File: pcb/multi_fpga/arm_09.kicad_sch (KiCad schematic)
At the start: 16 parts, among them U73 IM72D128V01XTMA1, U74 IM72D128V01XTMA1, U75 IM72D128V01XTMA1, U76 IM72D128V01XTMA1, U77 IM72D128V01XTMA1, U78 IM72D128V01XTMA1, U79 IM72D128V01XTMA1, U80 IM72D128V01XTMA1

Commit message: Fixed library and power issues.
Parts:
- C73, C74, C75, C76, C77, C78, C79, C80: symbol C -> multi_fpga:C
- U73, U74, U75, U76, U77, U78, U79, U80: symbol IM72D128 -> multi_fpga:IM72D128

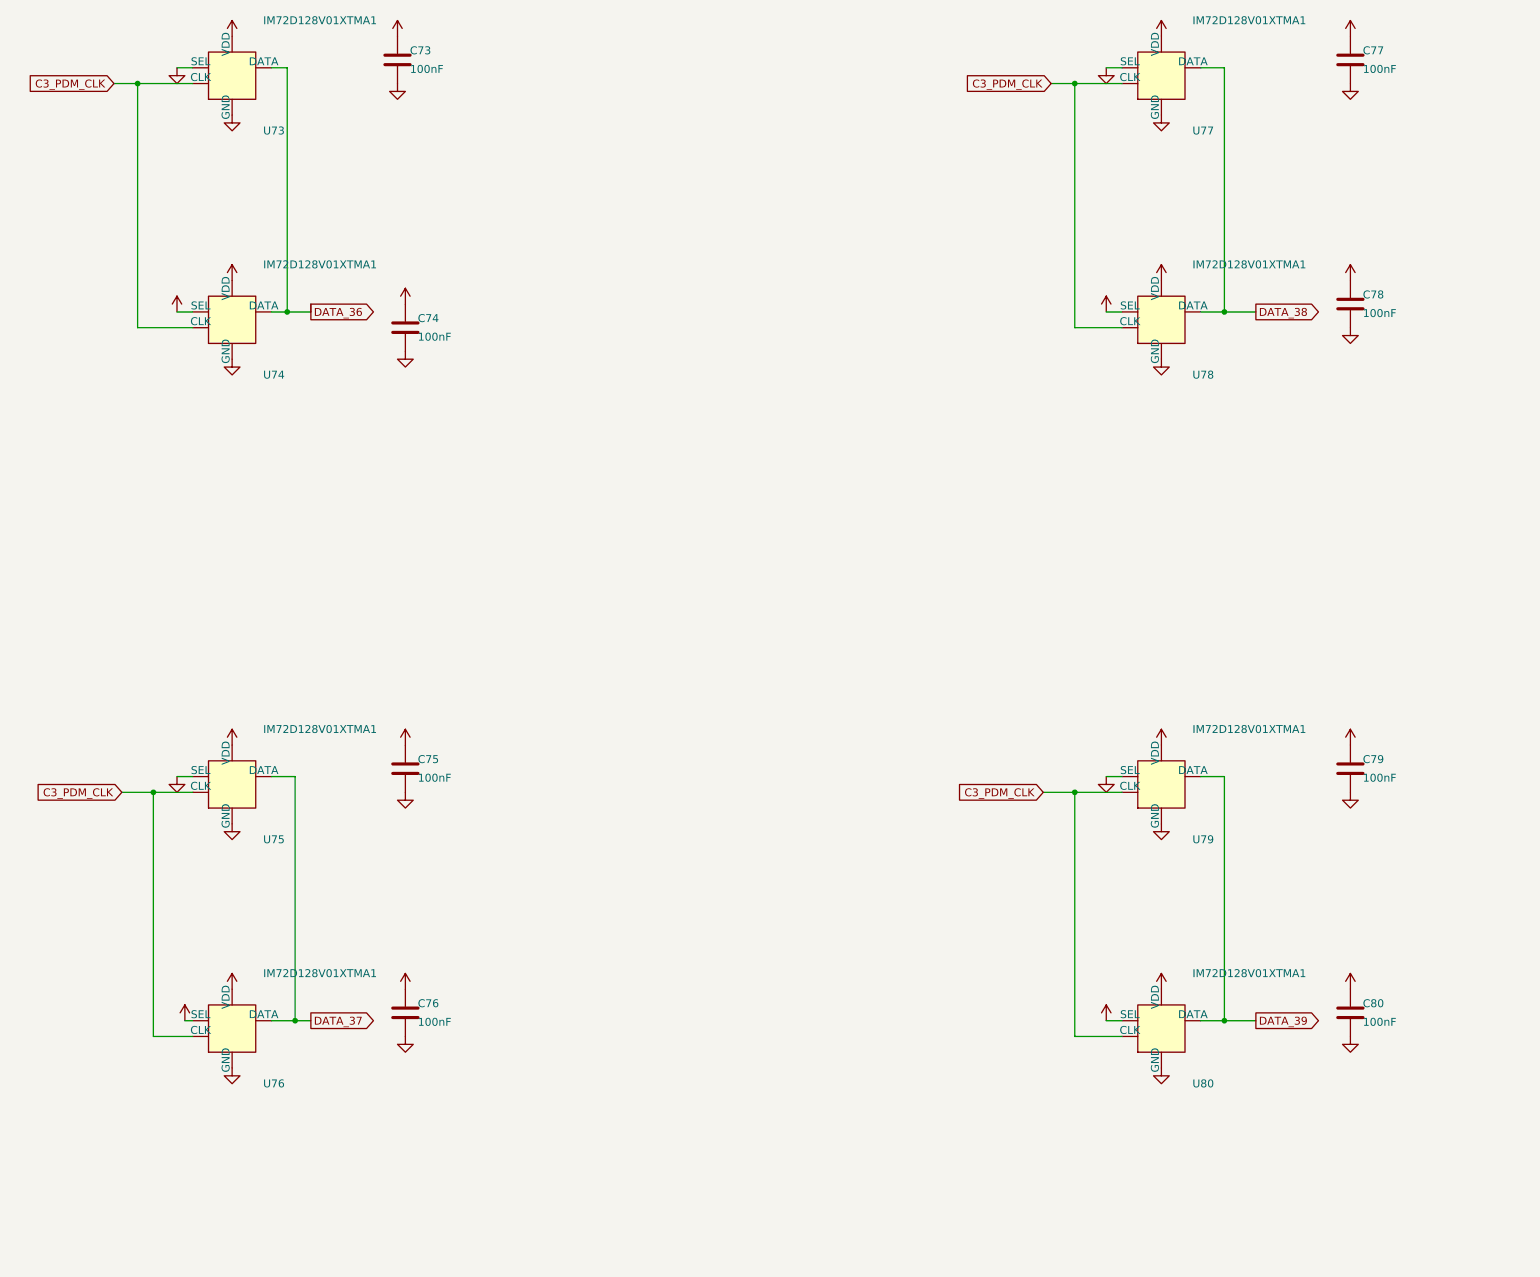
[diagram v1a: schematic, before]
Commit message: Fixed power and C ref des collisions.
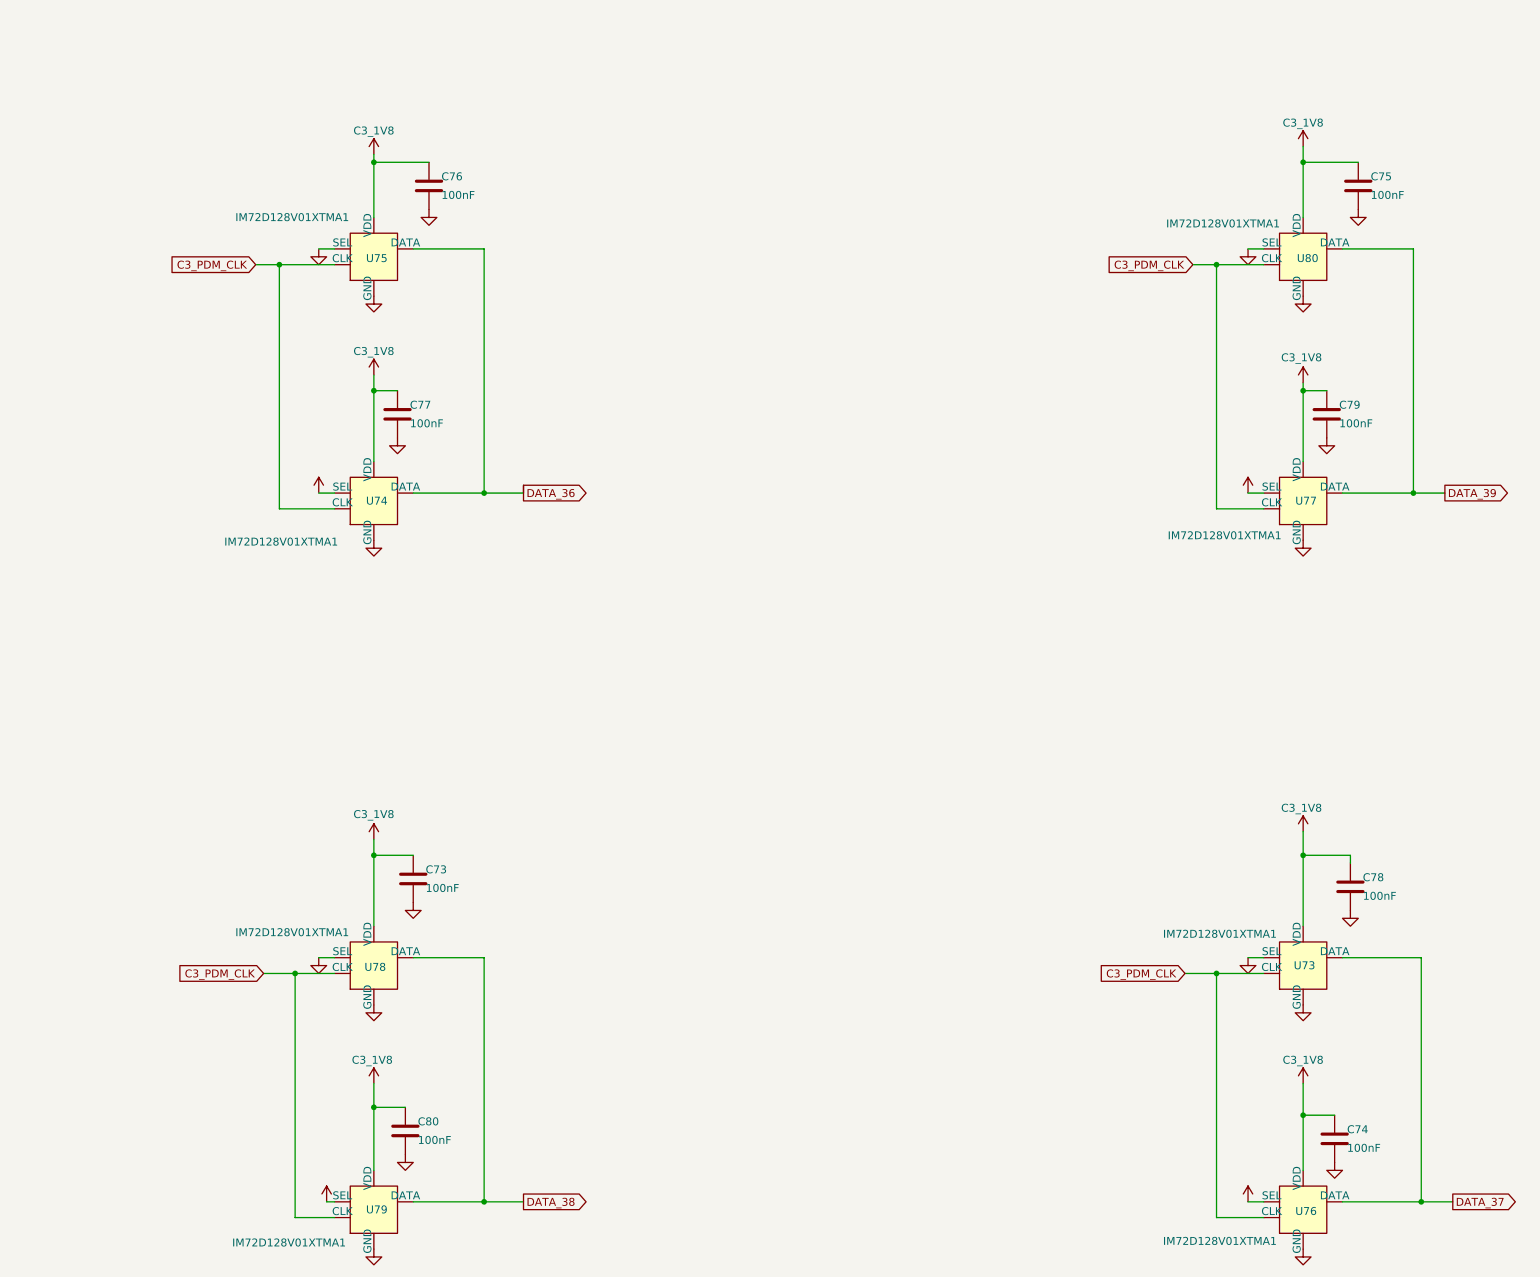
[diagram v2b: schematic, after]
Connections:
- net C3_1V8: now also U77.4 (SEL), U79.4 (SEL); no longer U78.4 (SEL), U80.4 (SEL)
- net DATA_36: now also U75.1 (DATA); no longer U73.1 (DATA)
- net DATA_37: now also U73.1 (DATA); no longer U75.1 (DATA)
- net DATA_38: now also U79.1 (DATA); no longer U77.1 (DATA)
- net DATA_39: now also U77.1 (DATA); no longer U79.1 (DATA)
- net GND: now also U78.4 (SEL), U80.4 (SEL); no longer U77.4 (SEL), U79.4 (SEL)

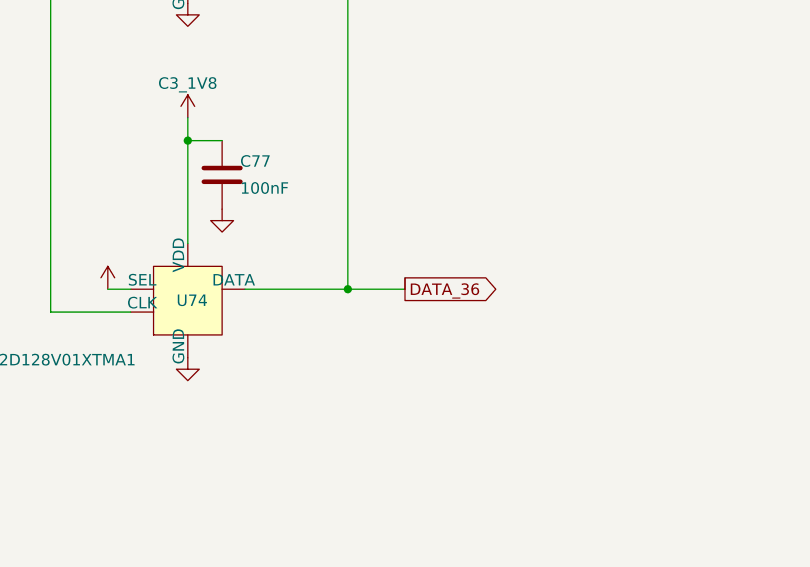
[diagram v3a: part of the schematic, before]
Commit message: Fixed regulator connection errors and dangling wire.
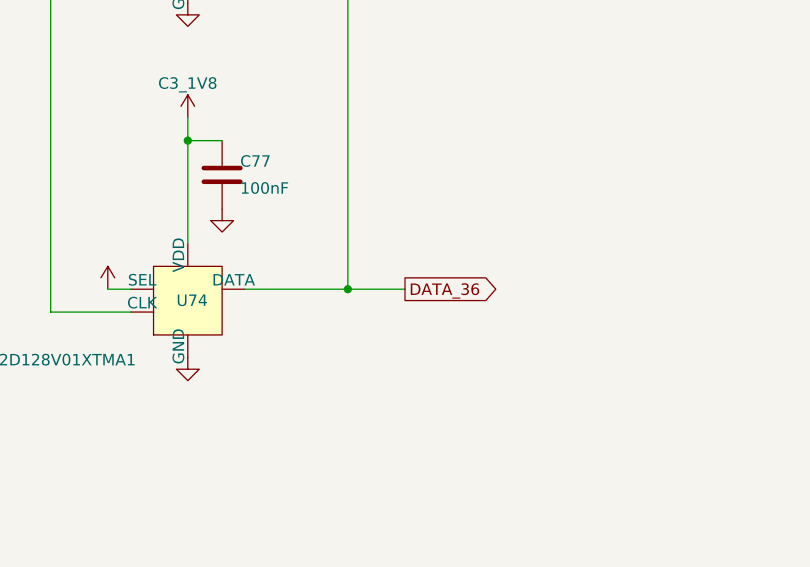
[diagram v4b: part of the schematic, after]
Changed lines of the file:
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@@
-	(wire
-		(pts
-			(xy 127 106.68) (xy 127 107.95)
-		)
-		(stroke
-			(width 0)
-			(type default)
-		)
-	)
 	(wire
 		(pts

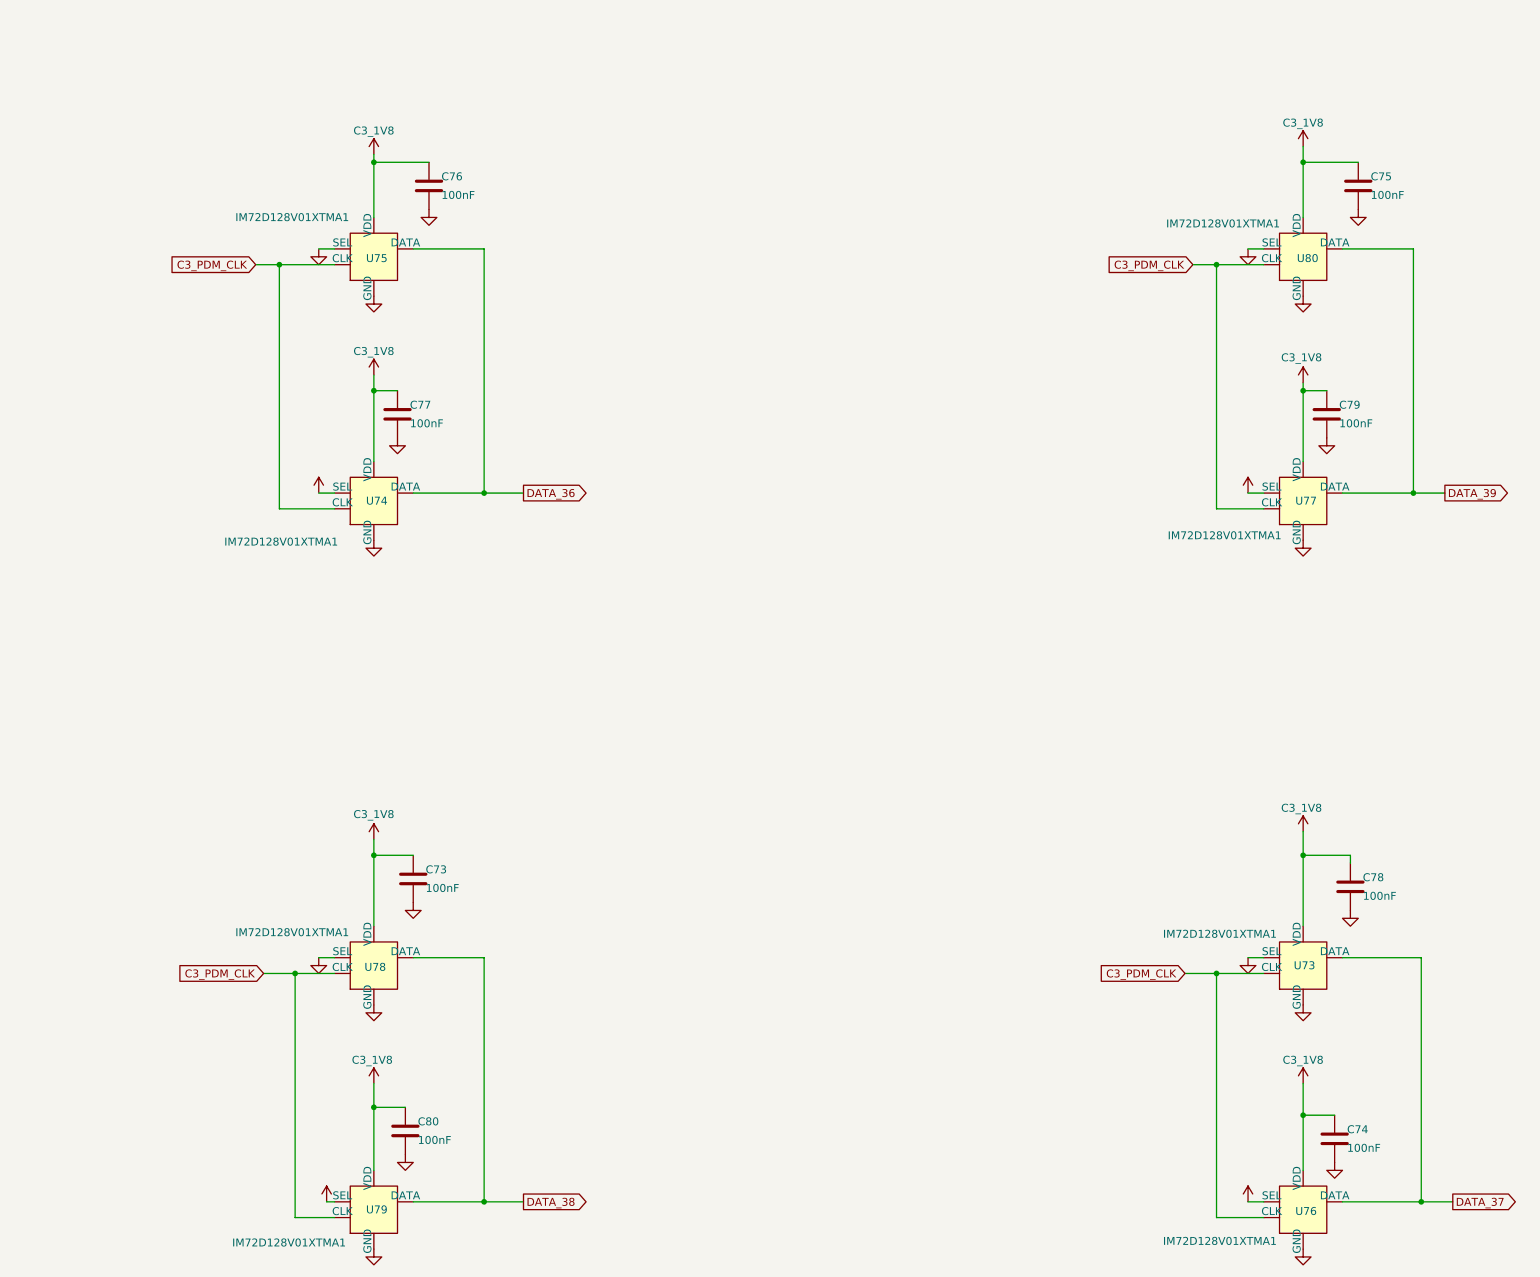
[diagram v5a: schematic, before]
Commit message: Global fix of res defs.
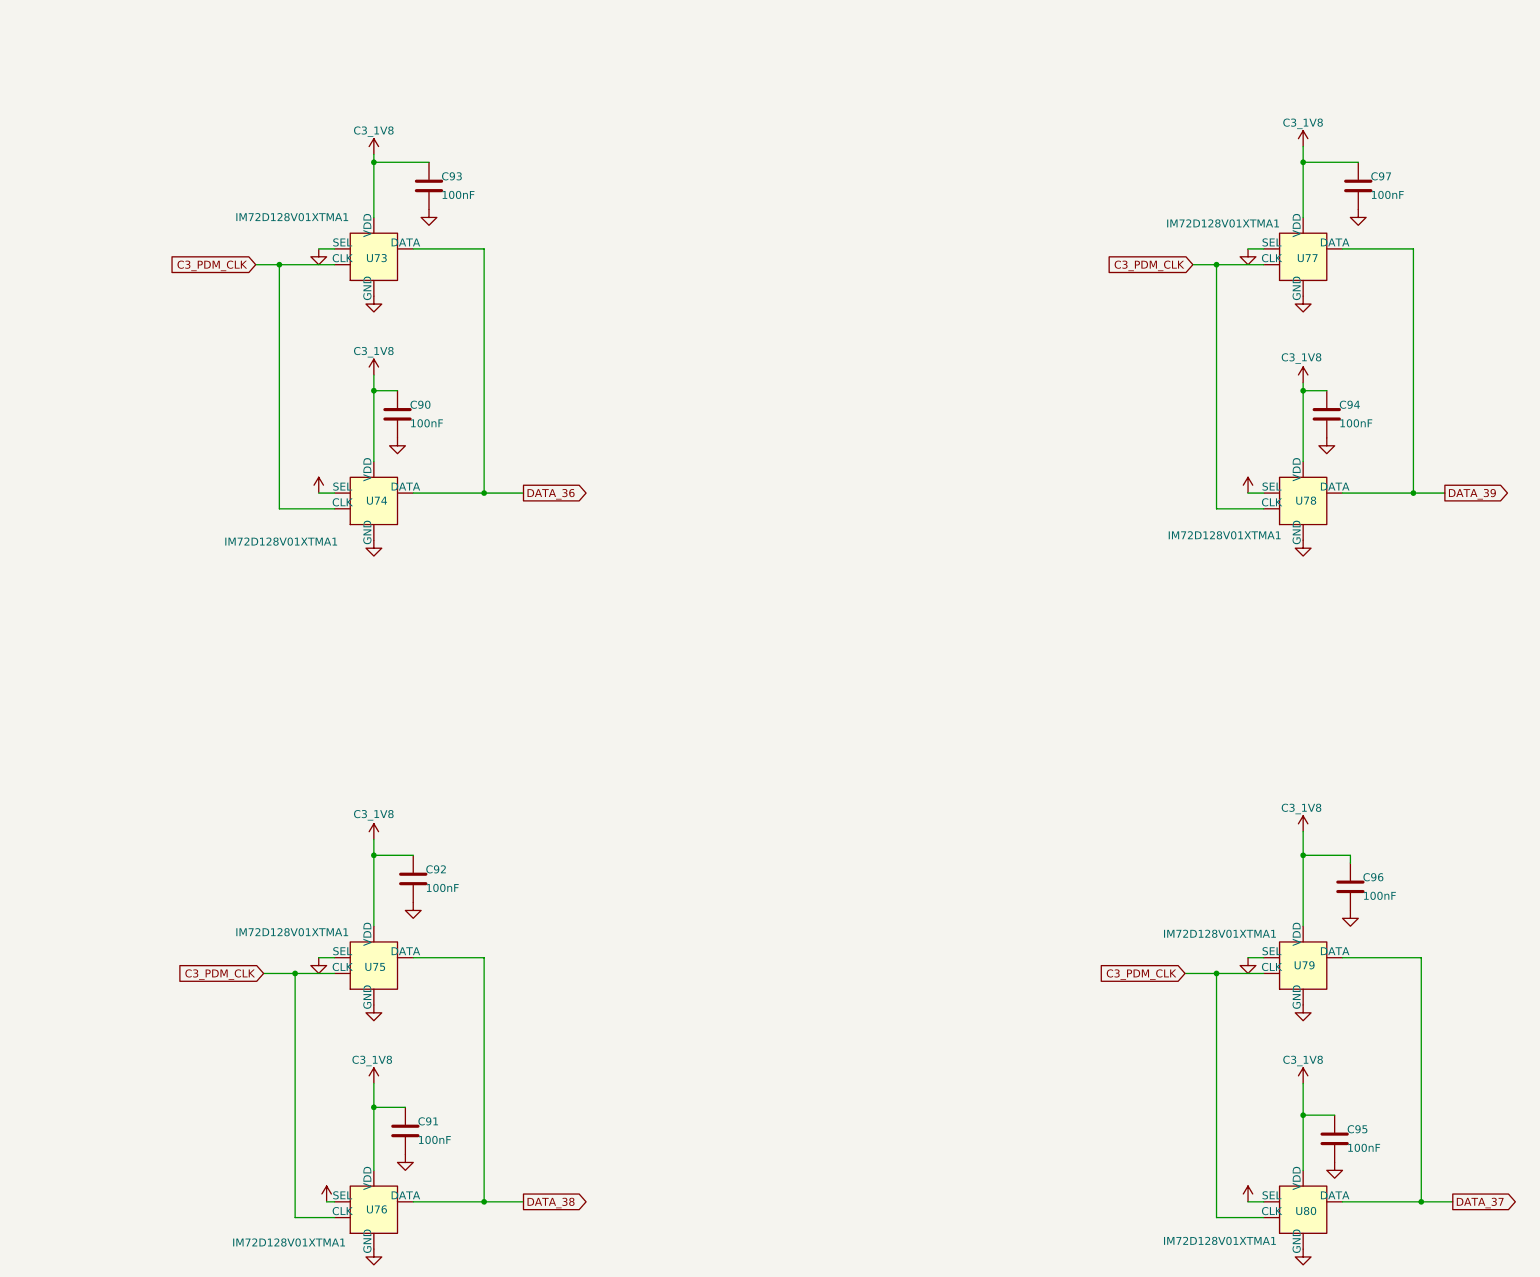
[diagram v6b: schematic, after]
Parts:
- renumbered C77 to C90, C80 to C91, C73 to C92, C76 to C93, C79 to C94, C74 to C95, C78 to C96, C75 to C97, U75 to U73, U78 to U75, U79 to U76, U80 to U77, U77 to U78, U73 to U79, U76 to U80

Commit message: Changed to use generic cap symbols and footprints.
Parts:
- C90, C91, C92, C93, C94, C95, C96, C97: symbol multi_fpga:C -> Device:C
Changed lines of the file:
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@@
 	)
 	(symbol
-		(lib_id "multi_fpga:C")
+		(lib_id "Device:C")
 		(at 107.95 210.82 0)
 		(unit 1)
@@
 		)
 		(property "Footprint" ""
-			(at 107.95 210.82 0)
+			(at 108.9152 214.63 0)
 			(hide yes)
 			(show_name no)
@@
 			)
 		)
-		(property "Description" "100 nF decoupling capacitor, 0402"
+		(property "Description" "Unpolarized capacitor"
 			(at 107.95 210.82 0)
 			(hide yes)
@@
 	)
 	(symbol
-		(lib_id "multi_fpga:C")
+		(lib_id "Device:C")
 		(at 257.81 212.09 0)
 		(unit 1)
@@
 		)
 		(property "Footprint" ""
-			(at 257.81 212.09 0)
+			(at 258.7752 215.9 0)
 			(hide yes)
 			(show_name no)
@@
 			)
 		)
-		(property "Description" "100 nF decoupling capacitor, 0402"
+		(property "Description" "Unpolarized capacitor"
 			(at 257.81 212.09 0)
 			(hide yes)
@@
 	)
 	(symbol
-		(lib_id "multi_fpga:C")
+		(lib_id "Device:C")
 		(at 111.76 58.42 0)
 		(unit 1)
@@
 		)
 		(property "Footprint" ""
-			(at 111.76 58.42 0)
+			(at 112.7252 62.23 0)
 			(hide yes)
 			(show_name no)
@@
 			)
 		)
-		(property "Description" "100 nF decoupling capacitor, 0402"
+		(property "Description" "Unpolarized capacitor"
 			(at 111.76 58.42 0)
 			(hide yes)
@@
 	)
 	(symbol
-		(lib_id "multi_fpga:C")
+		(lib_id "Device:C")
 		(at 109.22 170.18 0)
 		(unit 1)
@@
 		)
 		(property "Footprint" ""
-			(at 109.22 170.18 0)
+			(at 110.1852 173.99 0)
 			(hide yes)
 			(show_name no)
@@
 			)
 		)
-		(property "Description" "100 nF decoupling capacitor, 0402"
+		(property "Description" "Unpolarized capacitor"
 			(at 109.22 170.18 0)
 			(hide yes)
@@
 	)
 	(symbol
-		(lib_id "multi_fpga:C")
+		(lib_id "Device:C")
 		(at 261.62 58.42 0)
 		(unit 1)
@@
 		)
 		(property "Footprint" ""
-			(at 261.62 58.42 0)
+			(at 262.5852 62.23 0)
 			(hide yes)
 			(show_name no)
@@
 			)
 		)
-		(property "Description" "100 nF decoupling capacitor, 0402"
+		(property "Description" "Unpolarized capacitor"
 			(at 261.62 58.42 0)
 			(hide yes)
@@
 	)
 	(symbol
-		(lib_id "multi_fpga:C")
+		(lib_id "Device:C")
 		(at 256.54 95.25 0)
 		(unit 1)
@@
 		)
 		(property "Footprint" ""
-			(at 256.54 95.25 0)
+			(at 257.5052 99.06 0)
 			(hide yes)
 			(show_name no)
@@
 			)
 		)
-		(property "Description" "100 nF decoupling capacitor, 0402"
+		(property "Description" "Unpolarized capacitor"
 			(at 256.54 95.25 0)
 			(hide yes)
@@
 	)
 	(symbol
-		(lib_id "multi_fpga:C")
+		(lib_id "Device:C")
 		(at 260.35 171.45 0)
 		(unit 1)
@@
 		)
 		(property "Footprint" ""
-			(at 260.35 171.45 0)
+			(at 261.3152 175.26 0)
 			(hide yes)
 			(show_name no)
@@
 			)
 		)
-		(property "Description" "100 nF decoupling capacitor, 0402"
+		(property "Description" "Unpolarized capacitor"
 			(at 260.35 171.45 0)
 			(hide yes)
@@
 	)
 	(symbol
-		(lib_id "multi_fpga:C")
+		(lib_id "Device:C")
 		(at 106.68 95.25 0)
 		(unit 1)
@@
 		)
 		(property "Footprint" ""
-			(at 106.68 95.25 0)
+			(at 107.6452 99.06 0)
 			(hide yes)
 			(show_name no)
@@
 			)
 		)
-		(property "Description" "100 nF decoupling capacitor, 0402"
+		(property "Description" "Unpolarized capacitor"
 			(at 106.68 95.25 0)
 			(hide yes)
